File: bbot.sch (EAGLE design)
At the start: 27 parts

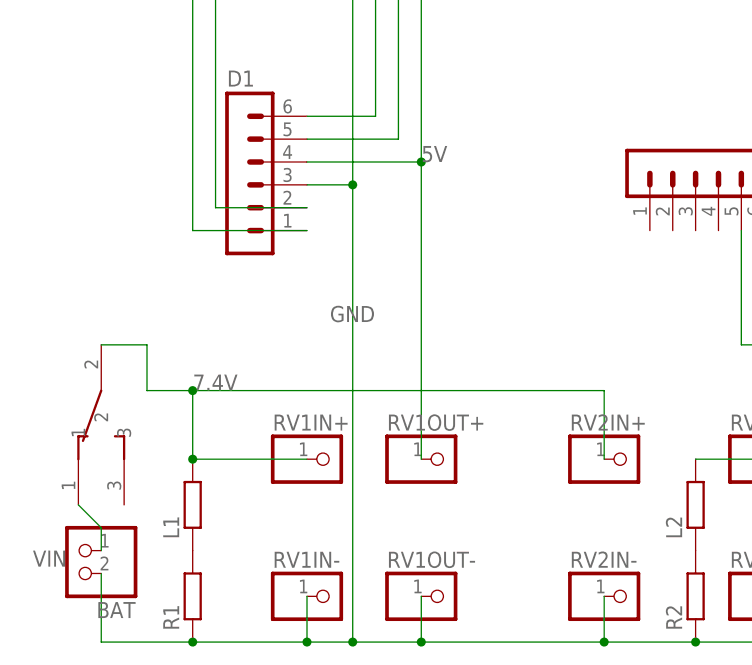
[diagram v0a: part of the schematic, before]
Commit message: added lm2596, everything is working
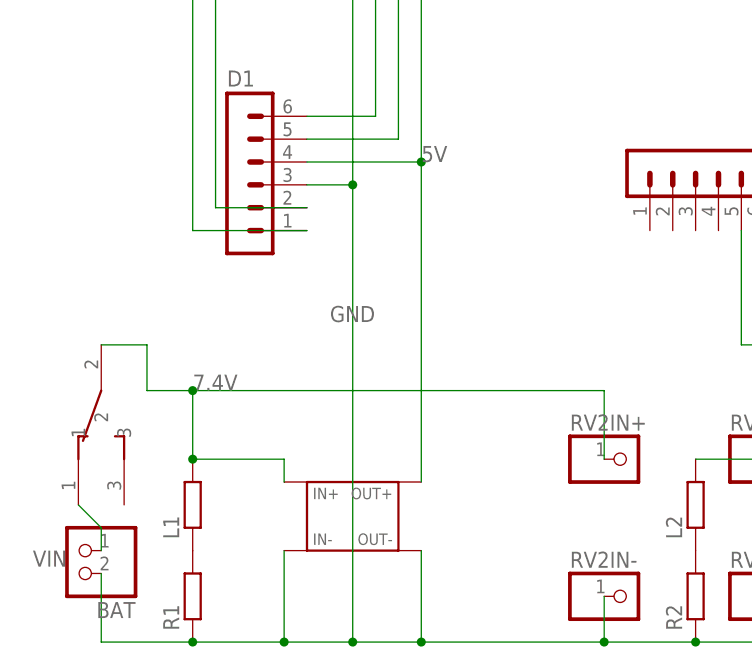
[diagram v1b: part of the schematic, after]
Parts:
- removed RV1IN+, RV1IN-, RV1OUT+, RV1OUT-: (no value), adafruit:PINHD-1X1
- added U$1: BB-LM2596, my-library:BB-LM2596
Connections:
- net 5V: now also U$1.OUT+; no longer RV1OUT+.1
- net 7.4V: now also U$1.IN+; no longer RV1IN+.1
- net GND: now also U$1.IN-, U$1.OUT-; no longer RV1IN-.1, RV1OUT-.1
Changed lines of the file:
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@@
 </class>
 </classes>
-<groups>
-<schematic_group name="RV"/>
-</groups>
 <parts>
-<part name="RV1IN+" library="adafruit" deviceset="PINHD-1X1" device=""/>
-<part name="RV1IN-" library="adafruit" deviceset="PINHD-1X1" device=""/>
-<part name="RV1OUT+" library="adafruit" deviceset="PINHD-1X1" device=""/>
-<part name="RV1OUT-" library="adafruit" deviceset="PINHD-1X1" device=""/>
 <part name="RV2IN-" library="adafruit" deviceset="PINHD-1X1" device=""/>
 <part name="RV2IN+" library="adafruit" deviceset="PINHD-1X1" device=""/>
 <part name="RV2OUT+" library="adafruit" deviceset="PINHD-1X1" device=""/>
 <part name="RV2OUT-" library="adafruit" deviceset="PINHD-1X1" device=""/>
-<part name="BT" library="my-library" library_urn="urn:adsk.eagle:library:37248401" deviceset="BB-HC06" device="" package3d_urn="urn:adsk.eagle:package:8337/1" value="5V"/>
+<part name="BT" library="my-library" library_urn="urn:adsk.eagle:library:37248401" deviceset="BB-HC06" device="" package3d_urn="urn:adsk.eagle:package:37312985/1" value="5V"/>
 <part name="D1" library="con-lstb" library_urn="urn:adsk.eagle:library:162" deviceset="MA06-1" device="" package3d_urn="urn:adsk.eagle:package:8340/1"/>
 <part name="D2" library="con-lstb" library_urn="urn:adsk.eagle:library:162" deviceset="MA06-1" device="" package3d_urn="urn:adsk.eagle:package:8340/1"/>
@@
 <part name="R2" library="my-library" library_urn="urn:adsk.eagle:library:37248401" deviceset="BB-RES" device="M0805" package3d_urn="urn:adsk.eagle:package:37248413/1"/>
 <part name="L2" library="my-library" library_urn="urn:adsk.eagle:library:37248401" deviceset="BB-RES" device="M0805" package3d_urn="urn:adsk.eagle:package:37248413/1"/>
+<part name="U$1" library="my-library" library_urn="urn:adsk.eagle:library:37248401" deviceset="BB-LM2596" device="" package3d_urn="urn:adsk.eagle:package:37312984/1"/>
 </parts>
 <sheets>
@@
 </plain>
 <instances>
-<instance part="RV1IN+" gate="G$1" x="38.1" y="0" smashed="yes" grouprefs="RV">
-<attribute name="NAME" x="31.75" y="3.175" size="1.778" layer="95"/>
-<attribute name="VALUE" x="31.75" y="-5.08" size="1.778" layer="96"/>
-</instance>
-<instance part="RV1IN-" gate="G$1" x="38.1" y="-15.24" smashed="yes" grouprefs="RV">
-<attribute name="NAME" x="31.75" y="-12.065" size="1.778" layer="95"/>
-<attribute name="VALUE" x="31.75" y="-20.32" size="1.778" layer="96"/>
-</instance>
-<instance part="RV1OUT+" gate="G$1" x="50.8" y="0" smashed="yes" grouprefs="RV">
-<attribute name="NAME" x="44.45" y="3.175" size="1.778" layer="95"/>
-<attribute name="VALUE" x="44.45" y="-5.08" size="1.778" layer="96"/>
-</instance>
-<instance part="RV1OUT-" gate="G$1" x="50.8" y="-15.24" smashed="yes" grouprefs="RV">
-<attribute name="NAME" x="44.45" y="-12.065" size="1.778" layer="95"/>
-<attribute name="VALUE" x="44.45" y="-20.32" size="1.778" layer="96"/>
-</instance>
 <instance part="RV2IN-" gate="G$1" x="71.12" y="-15.24" smashed="yes">
 <attribute name="NAME" x="64.77" y="-12.065" size="1.778" layer="95"/>
@@
 <attribute name="VALUE" x="82.042" y="-8.89" size="1.778" layer="96" rot="R90"/>
 </instance>
+<instance part="U$1" gate="G$1" x="53.34" y="-17.78" smashed="yes"/>
 </instances>
 <busses>
@@
 <label x="22.86" y="7.62" size="1.778" layer="95"/>
 <junction x="22.86" y="7.62"/>
-<pinref part="RV1IN+" gate="G$1" pin="1"/>
 <wire x1="22.86" y1="0" x2="22.86" y2="7.62" width="0.1524" layer="91"/>
-<wire x1="35.56" y1="0" x2="22.86" y2="0" width="0.1524" layer="91"/>
 <junction x="22.86" y="0"/>
+<wire x1="33.02" y1="0" x2="22.86" y2="0" width="0.1524" layer="91"/>
 <wire x1="17.78" y1="7.62" x2="17.78" y2="12.7" width="0.1524" layer="91"/>
 <pinref part="SW1" gate="G$1" pin="2"/>
 <wire x1="17.78" y1="12.7" x2="12.7" y2="12.7" width="0.1524" layer="91"/>
 <pinref part="L1" gate="G$1" pin="2"/>
+<pinref part="U$1" gate="G$1" pin="IN+"/>
+<wire x1="33.02" y1="-2.54" x2="33.02" y2="0" width="0.1524" layer="91"/>
 </segment>
 </net>
@@
 <wire x1="48.26" y1="66.04" x2="35.56" y2="66.04" width="0.1524" layer="91"/>
 <label x="48.26" y="33.02" size="1.778" layer="95"/>
-<pinref part="RV1OUT+" gate="G$1" pin="1"/>
-<wire x1="48.26" y1="33.02" x2="48.26" y2="0" width="0.1524" layer="91"/>
+<wire x1="48.26" y1="33.02" x2="48.26" y2="-2.54" width="0.1524" layer="91"/>
 <junction x="48.26" y="33.02"/>
+<pinref part="U$1" gate="G$1" pin="OUT+"/>
 </segment>
 </net>
@@
 <junction x="68.58" y="-20.32"/>
 <wire x1="48.26" y1="-20.32" x2="68.58" y2="-20.32" width="0.1524" layer="91"/>
-<pinref part="RV1OUT-" gate="G$1" pin="1"/>
-<wire x1="48.26" y1="-15.24" x2="48.26" y2="-20.32" width="0.1524" layer="91"/>
 <junction x="48.26" y="-20.32"/>
 <pinref part="D2" gate="1" pin="3"/>
@@
 <wire x1="40.64" y1="-20.32" x2="48.26" y2="-20.32" width="0.1524" layer="91"/>
 <junction x="40.64" y="-20.32"/>
-<pinref part="RV1IN-" gate="G$1" pin="1"/>
-<wire x1="35.56" y1="-20.32" x2="35.56" y2="-15.24" width="0.1524" layer="91"/>
-<wire x1="35.56" y1="-20.32" x2="40.64" y2="-20.32" width="0.1524" layer="91"/>
-<junction x="35.56" y="-20.32"/>
+<wire x1="33.02" y1="-20.32" x2="40.64" y2="-20.32" width="0.1524" layer="91"/>
+<junction x="33.02" y="-20.32"/>
 <wire x1="12.7" y1="-20.32" x2="22.86" y2="-20.32" width="0.1524" layer="91"/>
 <label x="38.1" y="15.24" size="1.778" layer="95"/>
-<wire x1="22.86" y1="-20.32" x2="35.56" y2="-20.32" width="0.1524" layer="91"/>
+<wire x1="22.86" y1="-20.32" x2="33.02" y2="-20.32" width="0.1524" layer="91"/>
 <wire x1="86.36" y1="-20.32" x2="93.98" y2="-20.32" width="0.1524" layer="91"/>
 <wire x1="93.98" y1="-20.32" x2="93.98" y2="15.24" width="0.1524" layer="91"/>
@@
 <pinref part="R2" gate="G$1" pin="1"/>
 <junction x="78.74" y="-20.32"/>
+<pinref part="U$1" gate="G$1" pin="OUT-"/>
+<wire x1="48.26" y1="-10.16" x2="48.26" y2="-20.32" width="0.1524" layer="91"/>
+<pinref part="U$1" gate="G$1" pin="IN-"/>
+<wire x1="33.02" y1="-20.32" x2="33.02" y2="-10.16" width="0.1524" layer="91"/>
 </segment>
 </net>
@@
 packages will not be understood (or retained) with this version.
 </note>
-<note version="9.5" severity="warning">
-Since Version 9.5, EAGLE supports persistent groups with
-schematics, and board files. Those persistent groups
-will not be understood (or retained) with this version.
-</note>
 <note version="8.4" severity="warning">

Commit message: added some tags to brd
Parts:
- removed RV2IN+, RV2IN-, RV2OUT+, RV2OUT-: (no value), adafruit:PINHD-1X1
- removed SV1, SV10, SV2, SV3, SV4, SV9: (no value), con-lstb:MA03-1
- removed U$1: BB-LM2596, my-library:BB-LM2596
- added 4, 5, 6, 9, A0, A1: BB-PIN3, my-library:BB-PIN3
- added LM2596: BB-LM2596, my-library:BB-LM2596
- added LM2596MINI: BB-LM2596MINI, my-library:BB-LM2596MINI
- BT: value 5V -> (none)
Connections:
- net 5V: now also LM2596.OUT+; no longer U$1.OUT+
- net 5V-A: now also 4.5V, 5.5V, 6.5V, 9.5V, A0.5V, A1.5V; no longer SV1.2, SV10.2, SV2.2, SV3.2, SV4.2, SV9.2
- net 7.4V: now also LM2596.IN+, LM2596MINI.IN+; no longer RV2IN+.1, U$1.IN+
- net GND: now also 4.GND, 5.GND, 6.GND, 9.GND, A0.GND, A1.GND, LM2596.IN-, LM2596.OUT-, LM2596MINI.IN-, LM2596MINI.OUT-; no longer RV2IN-.1, RV2OUT-.1, SV1.1, SV10.1, SV2.1, SV3.1, SV4.1, SV9.1, U$1.IN-, U$1.OUT-
- net N$14: now also 6.S; no longer SV2.3
- net N$15: now also 5.S; no longer SV3.3
- net N$16: now also 4.S; no longer SV4.3
- net N$17: now also A1.S, SV8.2; no longer SV8.6, SV9.3
- net N$18: now also A0.S, SV8.1; no longer SV10.3, SV8.5
- net N$5: now also 9.S; no longer SV1.3
- net VIN: now also LM2596MINI.OUT+; no longer RV2OUT+.1
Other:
- moved on the sheet: BT, L2, R2, SV7, SV8

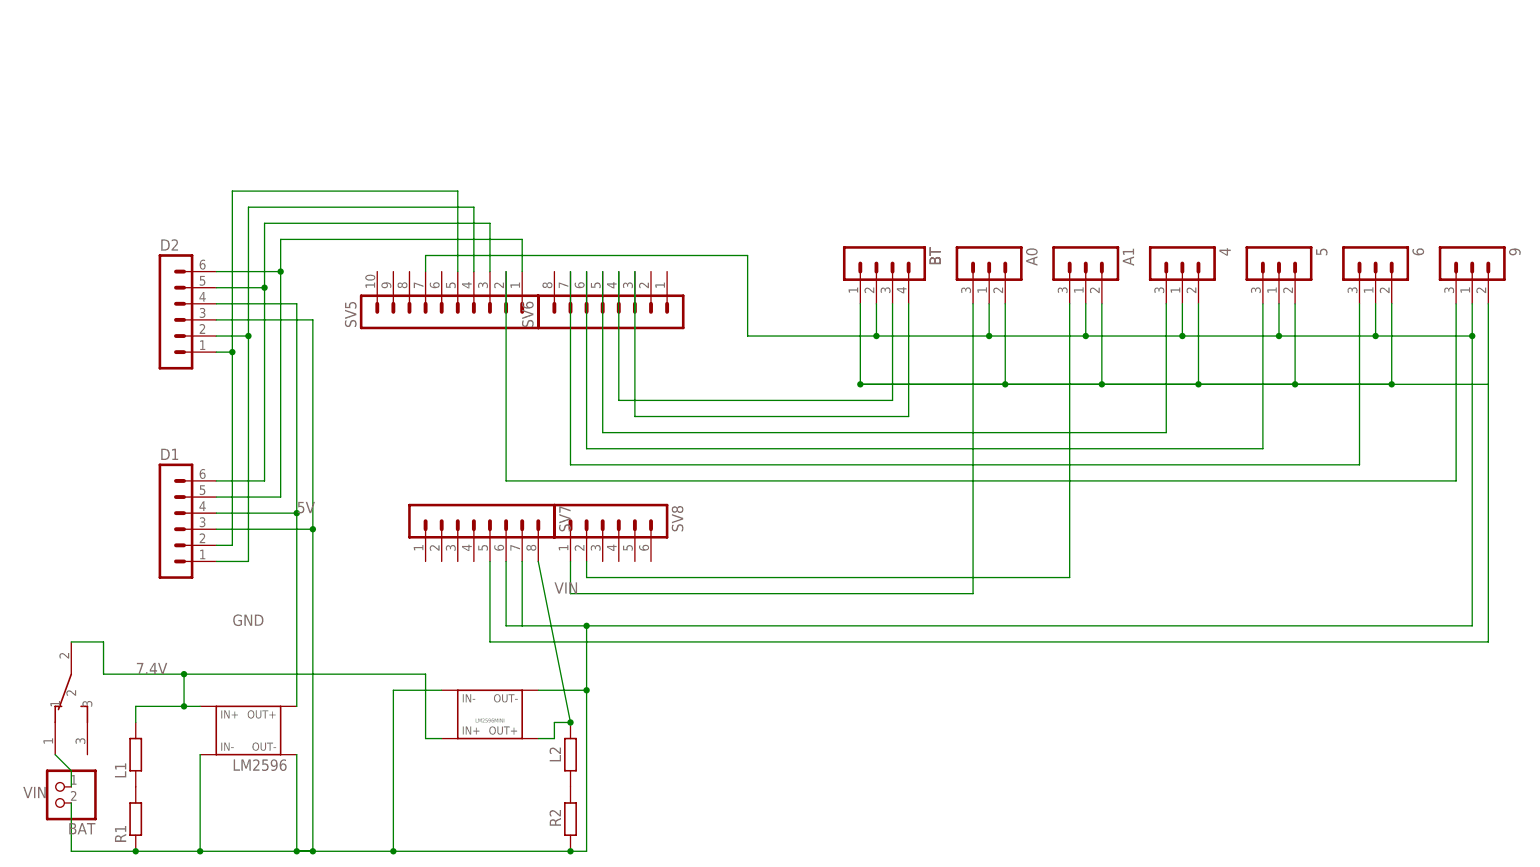
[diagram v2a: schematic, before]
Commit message: changed footprint arduino and h bridge, and added more tags
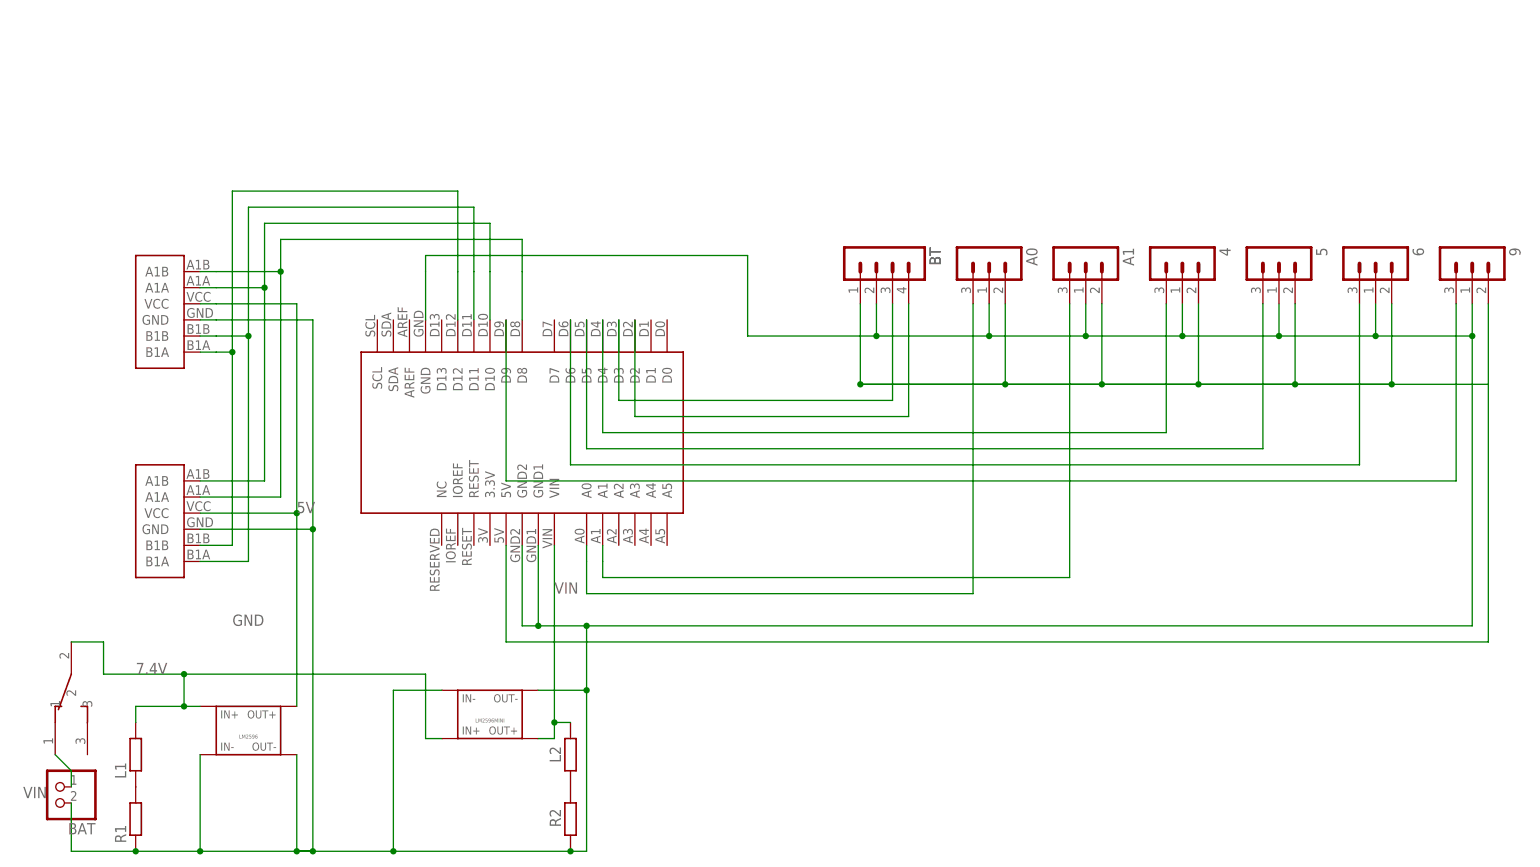
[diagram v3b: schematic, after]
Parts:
- removed D1, D2, SV8: (no value), con-lstb:MA06-1
- removed SV5: (no value), con-lstb:MA10-1
- removed SV6, SV7: (no value), con-lstb:MA08-1
- added U$1: BB-ARD, my-library:BB-ARD
- added U$2, U$3: BB-PTEH, my-library:BB-PTEH
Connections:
- net 5V: now also U$2.VCC, U$3.VCC; no longer D1.4, D2.4
- net 5V-A: now also U$1.5V; no longer SV7.5
- net GND: now also U$1.GND, U$1.GND1, U$1.GND2, U$2.GND, U$3.GND; no longer D1.3, D2.3, SV5.7, SV7.6, SV7.7
- net N$1: now also U$1.D3; no longer SV6.4
- net N$11: now also U$1.D12, U$2.B1A, U$3.B1B; no longer D1.2, D2.1, SV5.5
- net N$12: now also U$1.D10, U$2.A1A, U$3.A1B; no longer D1.6, D2.5, SV5.3
- net N$13: now also U$1.D8, U$2.A1B, U$3.A1A; no longer D1.5, D2.6, SV5.1
- net N$14: now also U$1.D6; no longer SV6.7
- net N$15: now also U$1.D5; no longer SV6.6
- net N$16: now also U$1.D4; no longer SV6.5
- net N$17: now also U$1.A1; no longer SV8.2
- net N$18: now also U$1.A0; no longer SV8.1
- net N$5: now also U$1.D9; no longer SV5.2
- net N$8: now also U$1.D11, U$2.B1B, U$3.B1A; no longer D1.1, D2.2, SV5.4
- net N$9: now also U$1.D2; no longer SV6.3
- net VIN: now also U$1.VIN; no longer SV7.8

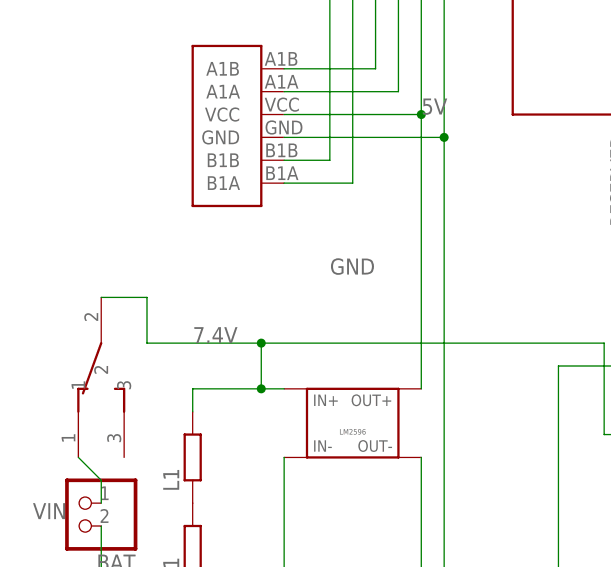
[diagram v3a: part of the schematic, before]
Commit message: added bp label and diode
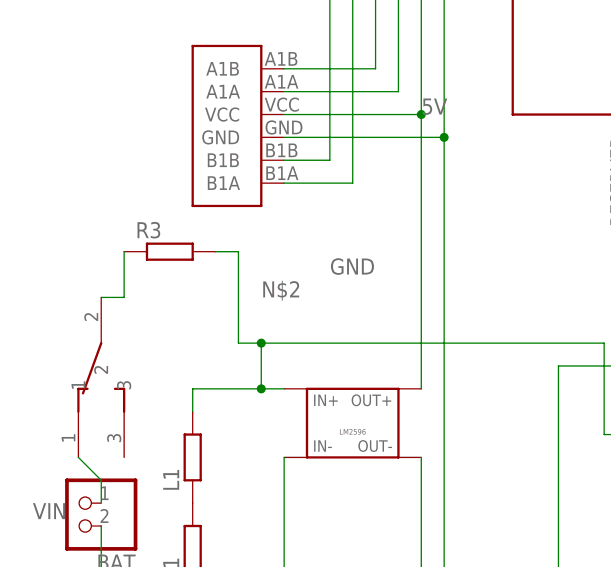
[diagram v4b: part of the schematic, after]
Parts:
- added R3: (no value), rcl:R-EU_0207/5V
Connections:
- new net N$2: R3.1, SW1.2
- net 7.4V: now also R3.2; no longer SW1.2
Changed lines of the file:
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@@
 <part name="U$2" library="my-library" library_urn="urn:adsk.eagle:library:37248401" deviceset="BB-PTEH" device=""/>
 <part name="U$3" library="my-library" library_urn="urn:adsk.eagle:library:37248401" deviceset="BB-PTEH" device=""/>
+<part name="R3" library="rcl" library_urn="urn:adsk.eagle:library:334" deviceset="R-EU_" device="0207/5V" package3d_urn="urn:adsk.eagle:package:23502/1"/>
 </parts>
 <sheets>
@@
 <instance part="U$2" gate="G$1" x="25.4" y="55.88" smashed="yes"/>
 <instance part="U$3" gate="G$1" x="25.4" y="22.86" smashed="yes"/>
+<instance part="R3" gate="G$1" x="20.32" y="17.78" smashed="yes">
+<attribute name="NAME" x="16.51" y="19.2786" size="1.778" layer="95"/>
+<attribute name="VALUE" x="16.51" y="14.478" size="1.778" layer="96"/>
+</instance>
 </instances>
 <busses>
@@
 <net name="7.4V" class="0">
 <segment>
-<wire x1="17.78" y1="7.62" x2="30.48" y2="7.62" width="0.1524" layer="91"/>
+<wire x1="27.94" y1="7.62" x2="30.48" y2="7.62" width="0.1524" layer="91"/>
 <wire x1="30.48" y1="7.62" x2="68.58" y2="7.62" width="0.1524" layer="91"/>
-<label x="22.86" y="7.62" size="1.778" layer="95"/>
-<wire x1="17.78" y1="7.62" x2="17.78" y2="12.7" width="0.1524" layer="91"/>
-<pinref part="SW1" gate="G$1" pin="2"/>
-<wire x1="17.78" y1="12.7" x2="12.7" y2="12.7" width="0.1524" layer="91"/>
 <pinref part="LM2596" gate="G$1" pin="IN+"/>
 <wire x1="33.02" y1="2.54" x2="30.48" y2="2.54" width="0.1524" layer="91"/>
@@
 <wire x1="68.58" y1="-2.54" x2="71.12" y2="-2.54" width="0.1524" layer="91"/>
 <pinref part="LM2596MINI" gate="G$1" pin="IN+"/>
+<pinref part="R3" gate="G$1" pin="2"/>
+<wire x1="25.4" y1="17.78" x2="27.94" y2="17.78" width="0.1524" layer="91"/>
+<wire x1="27.94" y1="17.78" x2="27.94" y2="7.62" width="0.1524" layer="91"/>
 </segment>
 </net>
@@
 </segment>
 </net>
+<net name="N$2" class="0">
+<segment>
+<pinref part="R3" gate="G$1" pin="1"/>
+<wire x1="15.24" y1="12.7" x2="15.24" y2="17.78" width="0.1524" layer="91"/>
+<pinref part="SW1" gate="G$1" pin="2"/>
+<wire x1="12.7" y1="12.7" x2="15.24" y2="12.7" width="0.1524" layer="91"/>
+<label x="30.48" y="12.7" size="1.778" layer="95"/>
+</segment>
+</net>
